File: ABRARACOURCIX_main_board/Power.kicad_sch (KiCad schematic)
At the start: 37 parts, among them J10 XT60PW-M, J11 Conn_01x02_Pin, J12 Conn_01x02_Pin, J8 XT60PW-M, J9 XT60PW-F, Q2 DSS20200L-7-PNP, Q3 IKD15N60R, Q4 NPN-DSS20201L-7, Q5 NTR4101PT1G, U3 Current_sens_ACS712ELCTR-20A-T, U4 AZ1117CH-3.3TRG1, U5 LMC6482AIMX/NOPB, U6 LMC6482AIMX/NOPB

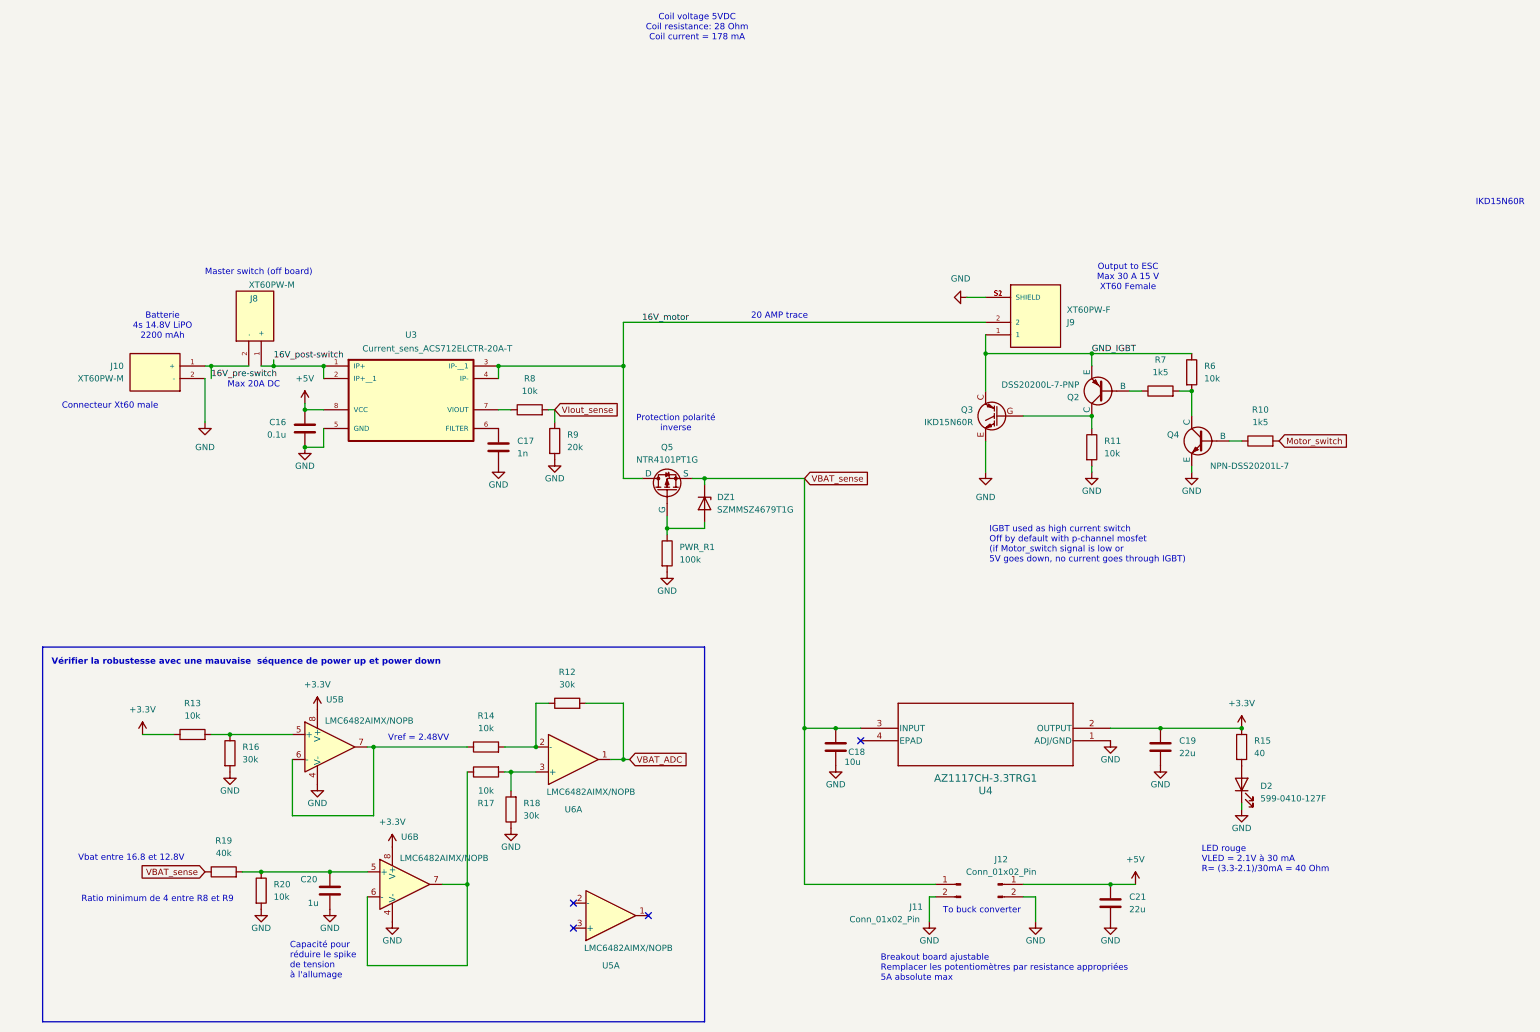
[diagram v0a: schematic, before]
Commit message: Documentation, lien digikey et part number assigné à toutes les composantes
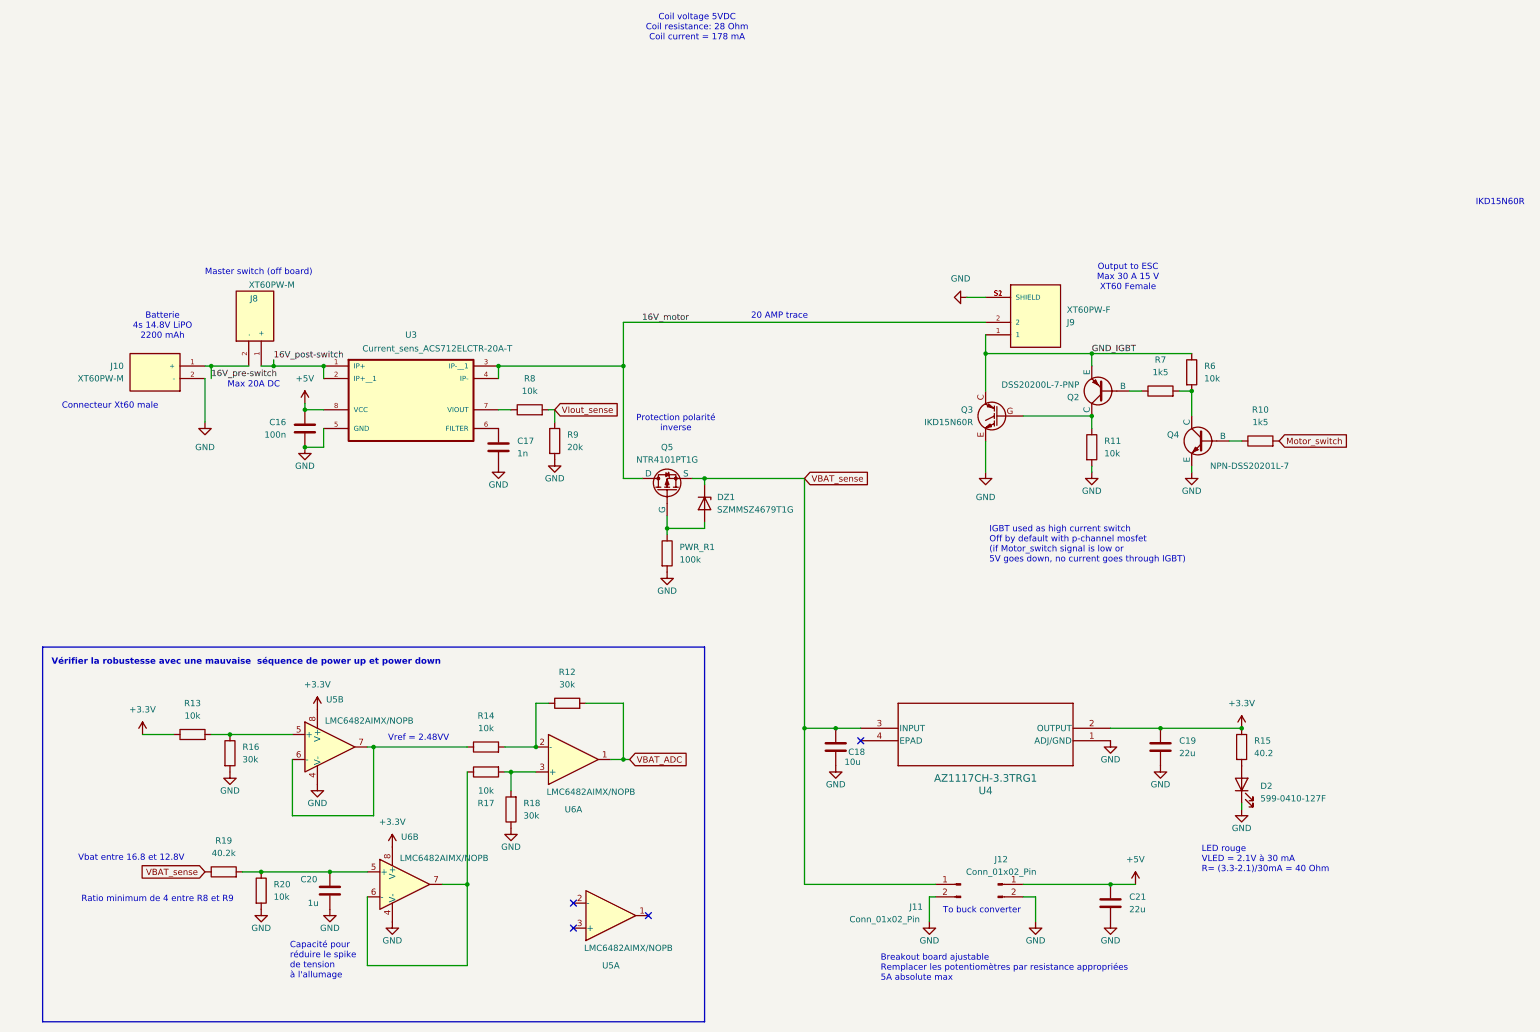
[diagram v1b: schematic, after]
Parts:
- C16: value 0.1u -> 100n; Digikey (none) -> https://www.digikey.ca/en/products/detail/walsin-technology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; Part number (none) -> 1292-1605-1-ND
- C17: Digikey (none) -> https://www.digikey.ca/en/products/detail/walsin-technology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; Part number (none) -> 1292-1598-1-ND
- C18: Digikey (none) -> https://www.digikey.ca/en/products/detail/walsin-technology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; Part number (none) -> 1292-1206X106K250CT-ND
- C19: Digikey (none) -> https://www.digikey.ca/en/products/detail/walsin-technology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; Part number (none) -> 1292-1206X226M160CT-ND
- C20: Digikey (none) -> https://www.digikey.ca/en/products/detail/walsin-technology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; Part number (none) -> 1292-1206B105K250CT-ND
- C21: footprint Resistor_SMD:R_0805_2012Metric -> Capacitor_SMD:C_1206_3216Metric_Pad1.33x1.80mm_HandSolder; Digikey (none) -> https://www.digikey.ca/en/products/detail/walsin-technology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; Part number (none) -> 1292-1206X226M160CT-ND
- D2: Part number (none) -> 350-599-0410-127FCT-ND
- DZ1: Digikey SZMMSZ4679T1GOSCT-ND -> https://www.digikey.ca/en/products/detail/onsemi/SZMMSZ4679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; Part number (none) -> SZMMSZ4679T1GOSCT-ND
- J10, J11, J12, J8, J9: now left out of the parts list
- PWR_R1: Digikey 541-100KUTR-ND -> https://www.digikey.ca/en/products/detail/bourns-inc/CR1206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; Part number (none) -> CR1206-JW-104ELFCT-ND
- Q2: Part number (none) -> DSS20200LDICT-ND
- Q3: Part number (none) -> NTR4101PT1GOSCT-ND
- Q4: Part number (none) -> DSS20201LDICT-ND
- Q5: Digikey NTR4101PT1GOSCT-ND -> https://www.digikey.ca/en/products/detail/onsemi/NTR4101PT1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; Part number (none) -> NTR4101PT1GOSCT-ND
- R10, R7: Digikey (none) -> https://www.digikey.ca/en/products/detail/bourns-inc/CR1206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; Part number (none) -> CR1206-JW-152ELFCT-ND
- R11, R13, R14, R17, R20, R6, R8: Digikey (none) -> https://www.digikey.ca/en/products/detail/bourns-inc/CR1206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; Part number (none) -> CR1206-JW-103ELFCT-ND
- R12, R16, R18: Digikey (none) -> https://www.digikey.ca/en/products/detail/bourns-inc/CR1206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; Part number (none) -> 118-CR1206-JW-303ELFCT-ND
- R15: value 40 -> 40.2; Digikey (none) -> https://www.digikey.ca/en/products/detail/bourns-inc/CR1206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; Part number (none) -> 118-CR1206-FX-40R2ELFCT-ND
- R19: value 40k -> 40.2k; Digikey (none) -> https://www.digikey.ca/en/products/detail/bourns-inc/CR1206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; Part number (none) -> 118-CR1206-FX-4022ELFCT-ND
- R9: Digikey (none) -> https://www.digikey.ca/en/products/detail/bourns-inc/CR1206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; Part number (none) -> 118-CR1206-JW-203ELFCT-ND
- U3: Digikey (none) -> https://www.digikey.ca/en/products/detail/allegro-microsyst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; Part number (none) -> 620-1190-1-ND
- U4: Digikey (none) -> https://www.digikey.ca/en/products/detail/diodes-incorporat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; Part number (none) -> AZ1117CH-3.3TRG1DICT-ND

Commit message: Liste des modifs pour la V2
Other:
- note added: "100 mV/A et ratio de diviseur de tension de 2/3"
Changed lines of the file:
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@@
+		)
+	)
+	(text "100 mV/A et ratio de diviseur de tension de 2/3 "
+		(exclude_from_sim no)
+		(at 99.314 62.992 0)
+		(effects
+			(font
+				(size 1.27 1.27)
+			)
 		)
 	)
